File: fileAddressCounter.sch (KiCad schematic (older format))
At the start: 16 parts, among them U13 CD74AC161M, U14 CD74AC161M, U16 CD74AC161M, U17 CD74AC161M, U18 74AHC1G04, U19 CD74AC161M, U20 CD74AC161M, U38 74AHC1G04, U39 74AHC1G04

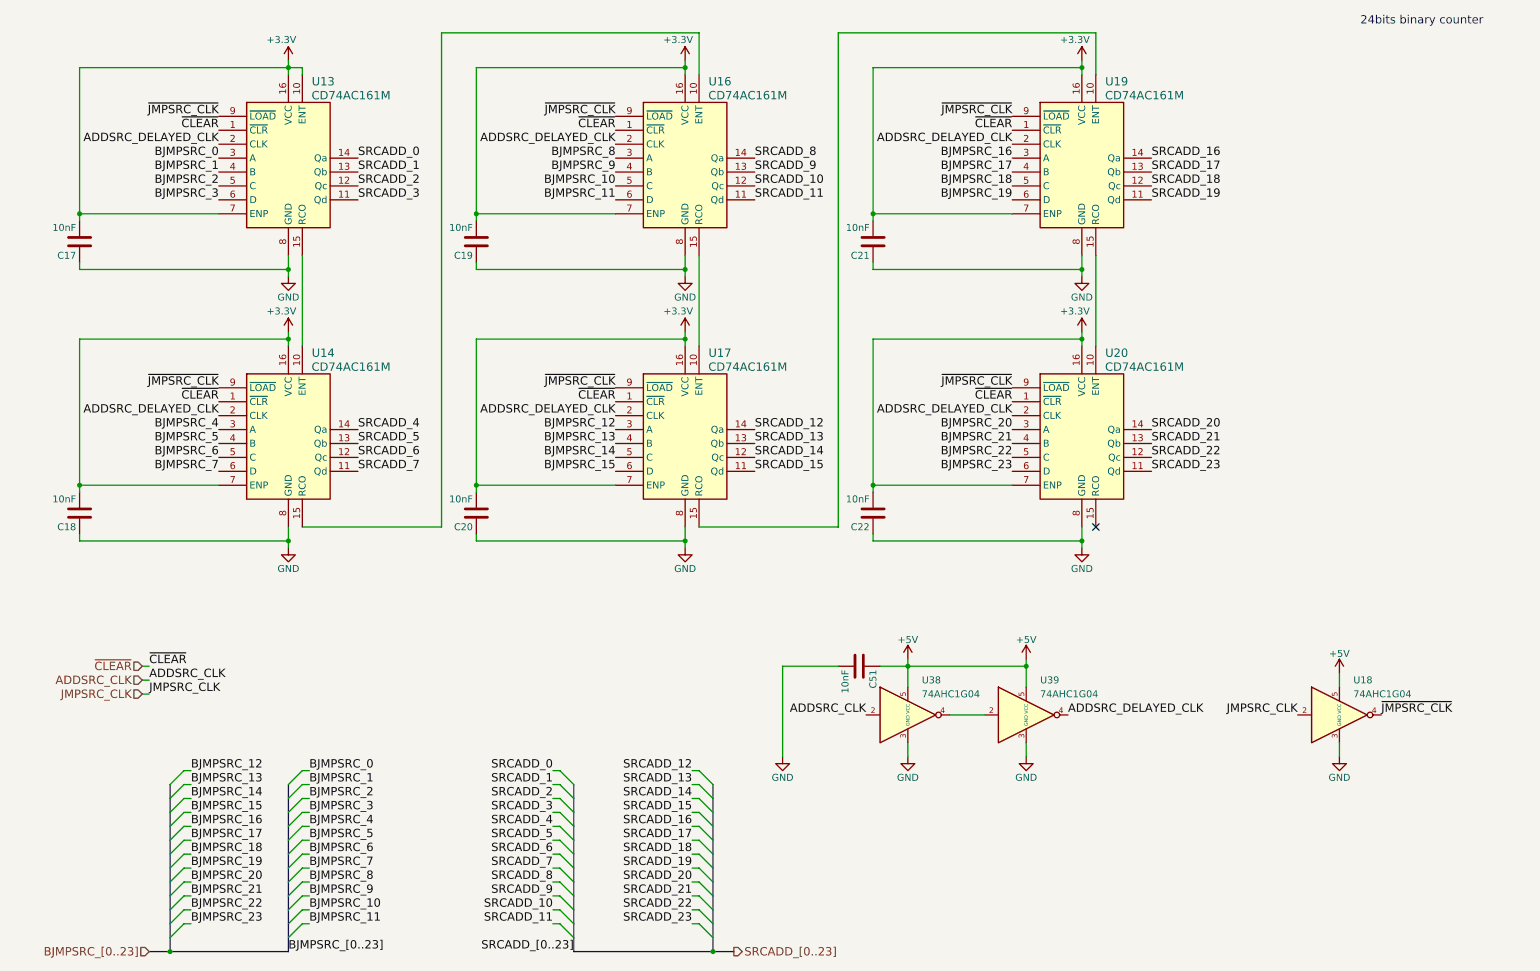
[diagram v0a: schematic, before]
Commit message: Removing ADDSCR_CLK delay #9
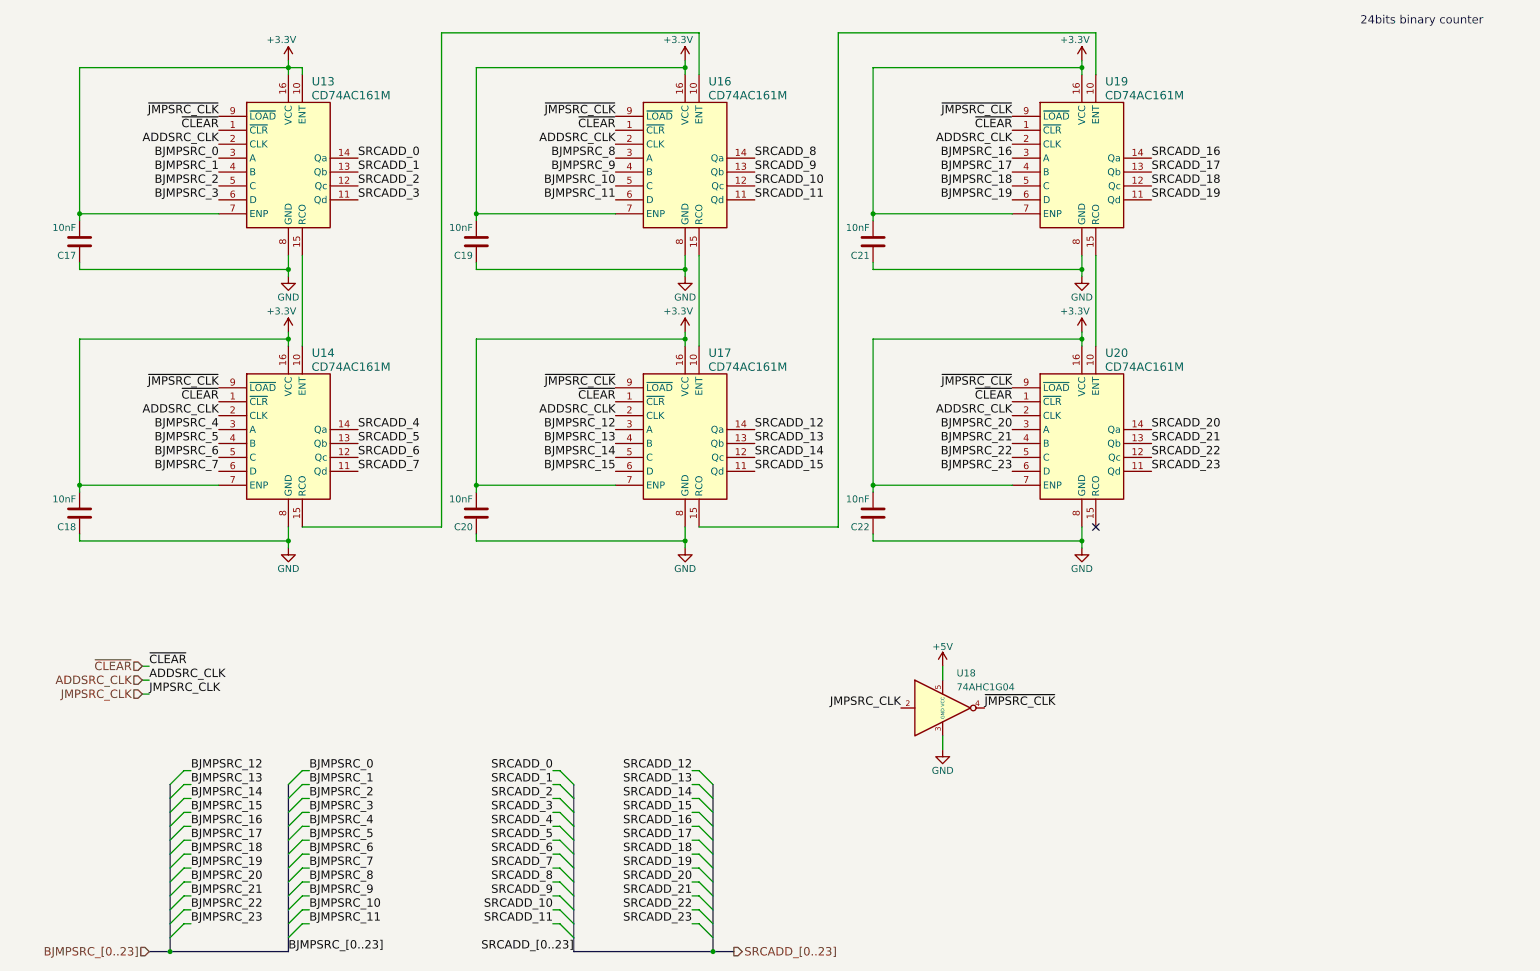
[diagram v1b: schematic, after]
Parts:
- removed C51: 10nF, Capacitor_SMD:C_0805_2012Metric, symbol Device:C
- removed U38, U39: 74AHC1G04, Package_TO_SOT_SMD:SOT-23-5, symbol Custom:74AHC1G04
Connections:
- net ADDSRC_DELAYED_CLK is gone; now on net ADDSRC_CLK: U13.2 (CLK), U14.2 (CLK), U16.2 (CLK), U17.2 (CLK), U19.2 (CLK), U20.2 (CLK)
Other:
- moved on the sheet: U18
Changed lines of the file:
@@
 L power:GND #PWR083
 U 1 1 5BB5F937
-P 9950 5900
+P 7100 5850
 AR Path="/5BB5F937" Ref="#PWR083"  Part="1"
 AR Path="/5A93FC93/5BB5F937" Ref="#PWR083"  Part="1"
-F 0 "#PWR083" H 9950 5650 50  0001 C CNN
-F 1 "GND" H 9950 5750 50  0000 C CNN
-F 2 "" H 9950 5900 50  0001 C CNN
-F 3 "" H 9950 5900 50  0001 C CNN
-	1    9950 5900
+F 0 "#PWR083" H 7100 5600 50  0001 C CNN
+F 1 "GND" H 7100 5700 50  0000 C CNN
+F 2 "" H 7100 5850 50  0001 C CNN
+F 3 "" H 7100 5850 50  0001 C CNN
+	1    7100 5850
 	1    0    0    -1
 $EndComp
@@
 L power:+5V #PWR084
 U 1 1 5BB5F9A2
-P 9950 5300
+P 7100 5250
 AR Path="/5BB5F9A2" Ref="#PWR084"  Part="1"
 AR Path="/5A93FC93/5BB5F9A2" Ref="#PWR084"  Part="1"
-F 0 "#PWR084" H 9950 5150 50  0001 C CNN
-F 1 "+5V" H 9950 5440 50  0000 C CNN
-F 2 "" H 9950 5300 50  0001 C CNN
-F 3 "" H 9950 5300 50  0001 C CNN
-	1    9950 5300
-	1    0    0    -1
-$EndComp
-Text Label 9650 5600 2    60   ~ 0
+F 0 "#PWR084" H 7100 5100 50  0001 C CNN
+F 1 "+5V" H 7100 5390 50  0000 C CNN
+F 2 "" H 7100 5250 50  0001 C CNN
+F 3 "" H 7100 5250 50  0001 C CNN
+	1    7100 5250
+	1    0    0    -1
+$EndComp
+Text Label 6800 5550 2    60   ~ 0
 JMPSRC_CLK
-Text Label 10250 5600 0    60   ~ 0
+Text Label 7400 5550 0    60   ~ 0
 ~JMPSRC_CLK
 Text Label 2550 6000 0    60   ~ 0
@@
 L Custom:74AHC1G04 U?
 U 1 1 5F9095CA
-P 9950 5600
+P 7100 5550
 AR Path="/5F9095CA" Ref="U?"  Part="1"
 AR Path="/5A93FC93/5F9095CA" Ref="U18"  Part="1"
-F 0 "U18" H 10050 5850 50  0000 L CNN
-F 1 "74AHC1G04" H 10050 5750 50  0000 L CNN
-F 2 "Package_TO_SOT_SMD:SOT-23-5" H 9950 5600 50  0001 C CNN
-F 3 "https://assets.nexperia.com/documents/data-sheet/74AHC_AHCT1G04.pdf" H 9950 5600 50  0001 C CNN
-	1    9950 5600
-	1    0    0    -1
-$EndComp
-Wire Wire Line
-	9950 5900 9950 5800
-Wire Wire Line
-	9950 5400 9950 5300
-$Comp
-L power:GND #PWR?
-U 1 1 5FB1C83D
-P 7700 5900
-AR Path="/5FB1C83D" Ref="#PWR?"  Part="1"
-AR Path="/5A93FC93/5FB1C83D" Ref="#PWR0163"  Part="1"
-F 0 "#PWR0163" H 7700 5650 50  0001 C CNN
-F 1 "GND" H 7700 5750 50  0000 C CNN
-F 2 "" H 7700 5900 50  0001 C CNN
-F 3 "" H 7700 5900 50  0001 C CNN
-	1    7700 5900
-	1    0    0    -1
-$EndComp
-$Comp
-L power:+5V #PWR?
-U 1 1 5FB1C843
-P 7700 5200
-AR Path="/5FB1C843" Ref="#PWR?"  Part="1"
-AR Path="/5A93FC93/5FB1C843" Ref="#PWR0164"  Part="1"
-F 0 "#PWR0164" H 7700 5050 50  0001 C CNN
-F 1 "+5V" H 7700 5340 50  0000 C CNN
-F 2 "" H 7700 5200 50  0001 C CNN
-F 3 "" H 7700 5200 50  0001 C CNN
-	1    7700 5200
-	1    0    0    -1
-$EndComp
-$Comp
-L Custom:74AHC1G04 U?
-U 1 1 5FB1C84B
-P 7700 5600
-AR Path="/5FB1C84B" Ref="U?"  Part="1"
-AR Path="/5A93FC93/5FB1C84B" Ref="U39"  Part="1"
-F 0 "U39" H 7800 5850 50  0000 L CNN
-F 1 "74AHC1G04" H 7800 5750 50  0000 L CNN
-F 2 "Package_TO_SOT_SMD:SOT-23-5" H 7700 5600 50  0001 C CNN
-F 3 "https://assets.nexperia.com/documents/data-sheet/74AHC_AHCT1G04.pdf" H 7700 5600 50  0001 C CNN
-	1    7700 5600
-	1    0    0    -1
-$EndComp
-Wire Wire Line
-	7700 5900 7700 5800
-$Comp
-L power:GND #PWR?
-U 1 1 5FB2A8C2
-P 6850 5900
-AR Path="/5FB2A8C2" Ref="#PWR?"  Part="1"
-AR Path="/5A93FC93/5FB2A8C2" Ref="#PWR0165"  Part="1"
-F 0 "#PWR0165" H 6850 5650 50  0001 C CNN
-F 1 "GND" H 6850 5750 50  0000 C CNN
-F 2 "" H 6850 5900 50  0001 C CNN
-F 3 "" H 6850 5900 50  0001 C CNN
-	1    6850 5900
-	1    0    0    -1
-$EndComp
-$Comp
-L power:+5V #PWR?
-U 1 1 5FB2A8C8
-P 6850 5200
-AR Path="/5FB2A8C8" Ref="#PWR?"  Part="1"
-AR Path="/5A93FC93/5FB2A8C8" Ref="#PWR0166"  Part="1"
-F 0 "#PWR0166" H 6850 5050 50  0001 C CNN
-F 1 "+5V" H 6850 5340 50  0000 C CNN
-F 2 "" H 6850 5200 50  0001 C CNN
-F 3 "" H 6850 5200 50  0001 C CNN
-	1    6850 5200
-	1    0    0    -1
-$EndComp
-$Comp
-L Custom:74AHC1G04 U?
-U 1 1 5FB2A8CE
-P 6850 5600
-AR Path="/5FB2A8CE" Ref="U?"  Part="1"
-AR Path="/5A93FC93/5FB2A8CE" Ref="U38"  Part="1"
-F 0 "U38" H 6950 5850 50  0000 L CNN
-F 1 "74AHC1G04" H 6950 5750 50  0000 L CNN
-F 2 "Package_TO_SOT_SMD:SOT-23-5" H 6850 5600 50  0001 C CNN
-F 3 "https://assets.nexperia.com/documents/data-sheet/74AHC_AHCT1G04.pdf" H 6850 5600 50  0001 C CNN
-	1    6850 5600
-	1    0    0    -1
-$EndComp
-Wire Wire Line
-	6850 5900 6850 5800
-Text Label 6550 5600 2    60   ~ 0
+F 0 "U18" H 7200 5800 50  0000 L CNN
+F 1 "74AHC1G04" H 7200 5700 50  0000 L CNN
+F 2 "Package_TO_SOT_SMD:SOT-23-5" H 7100 5550 50  0001 C CNN
+F 3 "https://assets.nexperia.com/documents/data-sheet/74AHC_AHCT1G04.pdf" H 7100 5550 50  0001 C CNN
+	1    7100 5550
+	1    0    0    -1
+$EndComp
+Wire Wire Line
+	7100 5850 7100 5750
+Wire Wire Line
+	7100 5350 7100 5250
+Text Label 7600 3450 2    60   ~ 0
 ADDSRC_CLK
-Text Label 8000 5600 0    60   ~ 0
-ADDSRC_DELAYED_CLK
-$Comp
-L Device:C C?
-U 1 1 5FB4378B
-P 6500 5250
-AR Path="/5FB4378B" Ref="C?"  Part="1"
-AR Path="/5A93FC93/5FB4378B" Ref="C51"  Part="1"
-F 0 "C51" H 6525 5350 50  0000 L CNN
-F 1 "10nF" H 6525 5150 50  0000 L CNN
-F 2 "Capacitor_SMD:C_0805_2012Metric" H 6538 5100 50  0001 C CNN
-F 3 "" H 6500 5250 50  0001 C CNN
-	1    6500 5250
-	0    1    1    0
-$EndComp
-Wire Wire Line
-	7700 5200 7700 5250
-Wire Wire Line
-	7700 5250 6850 5250
-Wire Wire Line
-	6850 5250 6850 5200
-Connection ~ 7700 5250
-Wire Wire Line
-	7700 5250 7700 5400
-Wire Wire Line
-	6850 5250 6850 5400
-Connection ~ 6850 5250
-Wire Wire Line
-	6850 5250 6650 5250
-Wire Wire Line
-	6350 5250 5950 5250
-Wire Wire Line
-	5950 5250 5950 5900
-$Comp
-L power:GND #PWR?
-U 1 1 5FB666FB
-P 5950 5900
-AR Path="/5FB666FB" Ref="#PWR?"  Part="1"
-AR Path="/5A93FC93/5FB666FB" Ref="#PWR0167"  Part="1"
-F 0 "#PWR0167" H 5950 5650 50  0001 C CNN
-F 1 "GND" H 5950 5750 50  0000 C CNN
-F 2 "" H 5950 5900 50  0001 C CNN
-F 3 "" H 5950 5900 50  0001 C CNN
-	1    5950 5900
-	1    0    0    -1
-$EndComp
-Wire Wire Line
-	7400 5600 7150 5600
 $Comp
 L Custom:CD74AC161M U19
@@
 	1    0    0    -1
 $EndComp
-Text Label 7600 1500 2    60   ~ 0
-ADDSRC_DELAYED_CLK
 Wire Wire Line
 	7600 2000 6600 2000
@@
 	1    0    0    -1
 $EndComp
-Text Label 7600 3450 2    60   ~ 0
-ADDSRC_DELAYED_CLK
 Wire Wire Line
 	7600 3950 6600 3950
@@
 	1    0    0    -1
 $EndComp
-Text Label 4750 1500 2    60   ~ 0
-ADDSRC_DELAYED_CLK
 Wire Wire Line
 	4750 2000 3750 2000
@@
 	3750 4000 3750 3950
 Connection ~ 3750 3950
-Text Label 4750 3450 2    60   ~ 0
-ADDSRC_DELAYED_CLK
 $Comp
 L Device:C C?
@@
 	1    0    0    -1
 $EndComp
-Text Label 1900 1500 2    60   ~ 0
-ADDSRC_DELAYED_CLK
 Wire Wire Line
 	1900 2000 900  2000
@@
 	900  4000 900  3950
 Connection ~ 900  3950
-Text Label 1900 3450 2    60   ~ 0
-ADDSRC_DELAYED_CLK
 Wire Wire Line
 	2500 1000 2500 950
@@
 	1    0    0    -1
 $EndComp
+Text Label 7600 1500 2    60   ~ 0
+ADDSRC_CLK
+Text Label 4750 1500 2    60   ~ 0
+ADDSRC_CLK
+Text Label 1900 1500 2    60   ~ 0
+ADDSRC_CLK
+Text Label 1900 3450 2    60   ~ 0
+ADDSRC_CLK
+Text Label 4750 3450 2    60   ~ 0
+ADDSRC_CLK
 Wire Bus Line
 	5450 6100 5450 7300
